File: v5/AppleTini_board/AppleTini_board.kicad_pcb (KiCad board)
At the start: 4 copper layers, 101.6 x 69.8 mm, 43 parts, among them J1 Conn_02x25_Counter_Clockwise, J2 Conn_02x14_Odd_Even, J3 Conn_02x14_Odd_Even, J4 Conn_02x05_Odd_Even, J5 Conn_02x05_Odd_Even, U1 74LS245, U2 74LS245, U3 74LS245, U4 74LCX07, U5 74LS245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

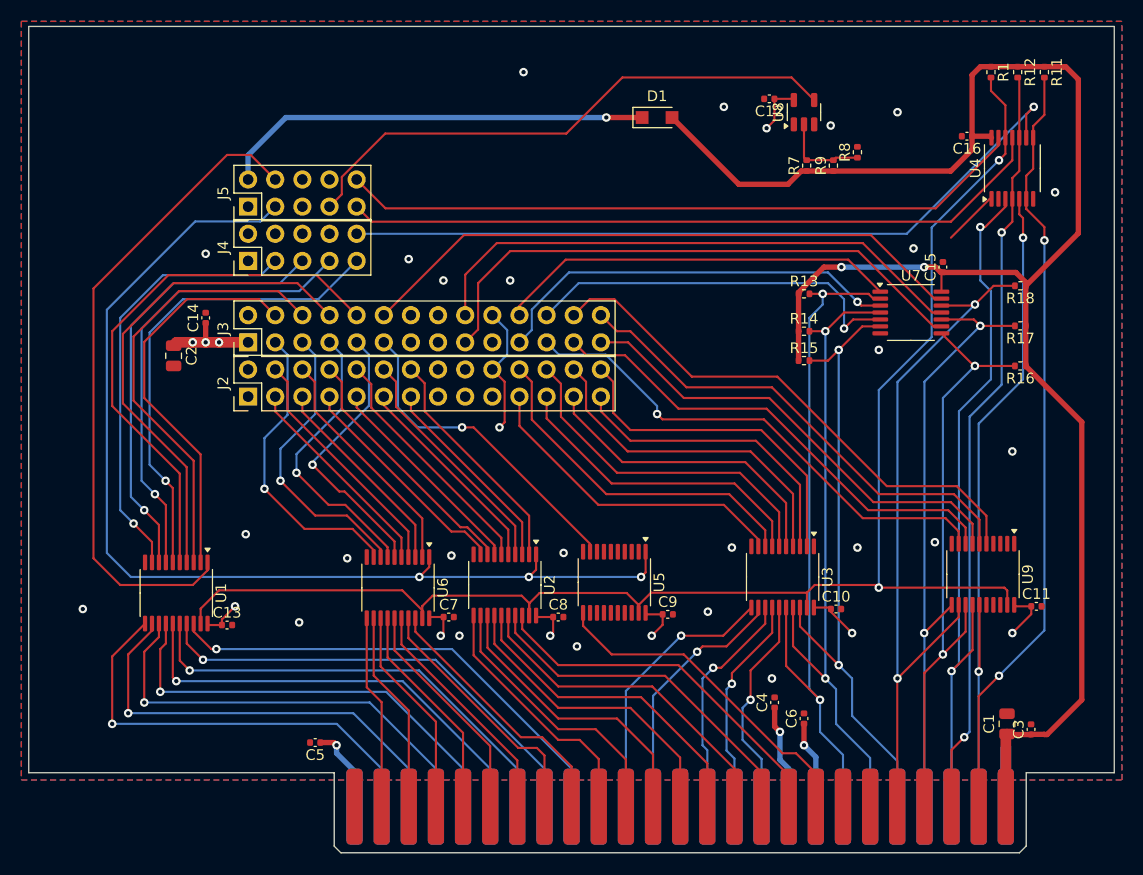
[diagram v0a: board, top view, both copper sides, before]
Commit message: v5.1 Kicad design, v5.1 Alchitry design
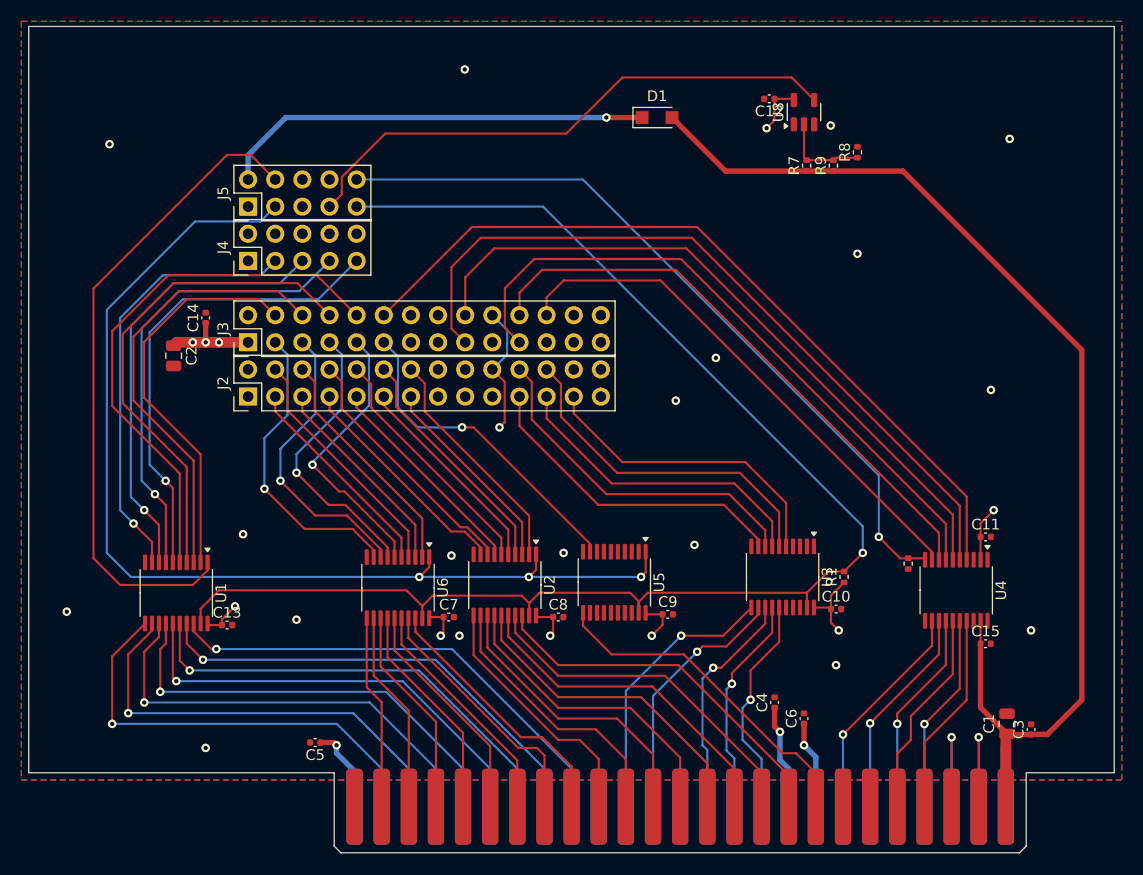
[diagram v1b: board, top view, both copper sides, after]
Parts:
- removed C16: C, Capacitor_SMD:C_0402_1005Metric
- removed R11, R12, R13, R14, R15, R16, R17, R18: R_US, Resistor_SMD:R_0402_1005Metric
- removed U7: 74LCX07, Package_SO:TSSOP-14_4.4x5mm_P0.65mm
- removed U9: 74LS245, Package_SO:TSSOP-20_4.4x6.5mm_P0.65mm
- added R2: R_US, Resistor_SMD:R_0402_1005Metric, F.Cu at (209.0, 121.2)
- U4: value 74LCX07 -> TXS0108EPWR; footprint Package_SO:TSSOP-14_4.4x5mm_P0.65mm -> Package_SO:TSSOP-20_4.4x6.5mm_P0.65mm
- U8: value 74LVC1G04 -> 74LVC1G04DBVRG
- moved R1 49.2 mm to (203.0, 122.5), turned to 90 degrees
- moved U4 39.8 mm to (213.5, 123.8), turned to -90 degrees
- moved C15 35.5 mm to (216.2, 128.8), turned to 0 degrees
- moved C11 8.05 mm to (216.2, 118.8)
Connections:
- J1 pad 23: /BUS_~{INTOUT} -> /BUS_~{INTINOUT}
- J1 pad 24: /BUS_~{DMAOUT} -> /BUS_~{DMAINOUT}
- J1 pad 27: /BUS_~{DMAIN} -> /BUS_~{DMAINOUT}
- J1 pad 28: /BUS_~{INTIN} -> /BUS_~{INTINOUT}
- R1 pad 1: +5V -> +3V3
- R1 pad 2: /~{OE} -> /C11
- U1 pad 19: /~{OE} -> /C11
- U2 pad 19: /~{OE} -> /C11
- U3 pad 16: /BUS_~{INH} -> GND
- U3 pad 17: /BUS_~{RES} -> GND
- U3 pad 18: /BUS_~{IRQ} -> GND
- U3 pad 19: /~{OE} -> /C11
- U3 pad 2: /B40 -> unconnected-(U3-A0-Pad2)
- U3 pad 3: /B39 -> unconnected-(U3-A1-Pad3)
- U3 pad 4: /B43 -> unconnected-(U3-A2-Pad4)
- U4 pad 1: GND -> unconnected-(U4-A1-Pad1)
- U4 pad 10: /BUS_~{INTOUT} -> /C12
- U4 pad 11: /C11 -> GND
- U4 pad 12: /~{OE} -> /BUS_~{INH}
- U4 pad 13: /C12 -> /BUS_~{RES}
- U4 pad 14: +5V -> /BUS_~{IRQ}
- U4 pad 2: unconnected-(U4-Pad2) -> +3V3
- U4 pad 3: /BUS_~{INTIN} -> unconnected-(U4-A2-Pad3)
- U4 pad 4: /BUS_~{INTOUT} -> /A14
- U4 pad 5: /BUS_~{DMAIN} -> /A24
- U4 pad 6: /BUS_~{DMAOUT} -> /A23
- U4 pad 7: GND -> /B3
- U4 pad 8: /BUS_~{DMAOUT} -> /B2
- U4 pad 9: /C39 -> /B5
- U5 pad 19: /~{OE} -> /C11
- U6 pad 19: /~{OE} -> /C11
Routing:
- net /~{OE}: track 141.8 -> 0.00 mm, vias 2 -> 0
- net /BUS_~{DMAOUT}: track 72.2 -> 0.00 mm, vias 2 -> 0
- net /C39: track 71.5 -> 0.00 mm, vias 1 -> 0
- net /BUS_~{INTOUT}: track 70.9 -> 0.00 mm, vias 2 -> 0
- net /C11: track 66.4 -> 135.4 mm, vias 0 -> 1
- net /BUS_~{INTIN}: track 67.1 -> 0.00 mm, vias 2 -> 0
- net /BUS_~{DMAIN}: track 65.0 -> 0.00 mm, vias 2 -> 0
- net +5V: track 160.6 -> 107.0 mm, vias 2 -> 0
- net /B8: track 50.3 -> 0.00 mm
- net /B6: track 47.5 -> 0.00 mm, vias 1 -> 0
- net /BUS_~{RDY}: track 66.9 -> 19.5 mm, vias 2 -> 0
- net /BUS_~{INH}: track 66.6 -> 20.8 mm, vias 2 -> 1
- net /B11: track 45.6 -> 0.00 mm
- net /B9: track 45.4 -> 0.00 mm
- net /B12: track 43.7 -> 0.00 mm
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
